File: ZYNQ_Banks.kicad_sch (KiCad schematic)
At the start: 15 parts, among them U1 XC7Z020-2CLG484I

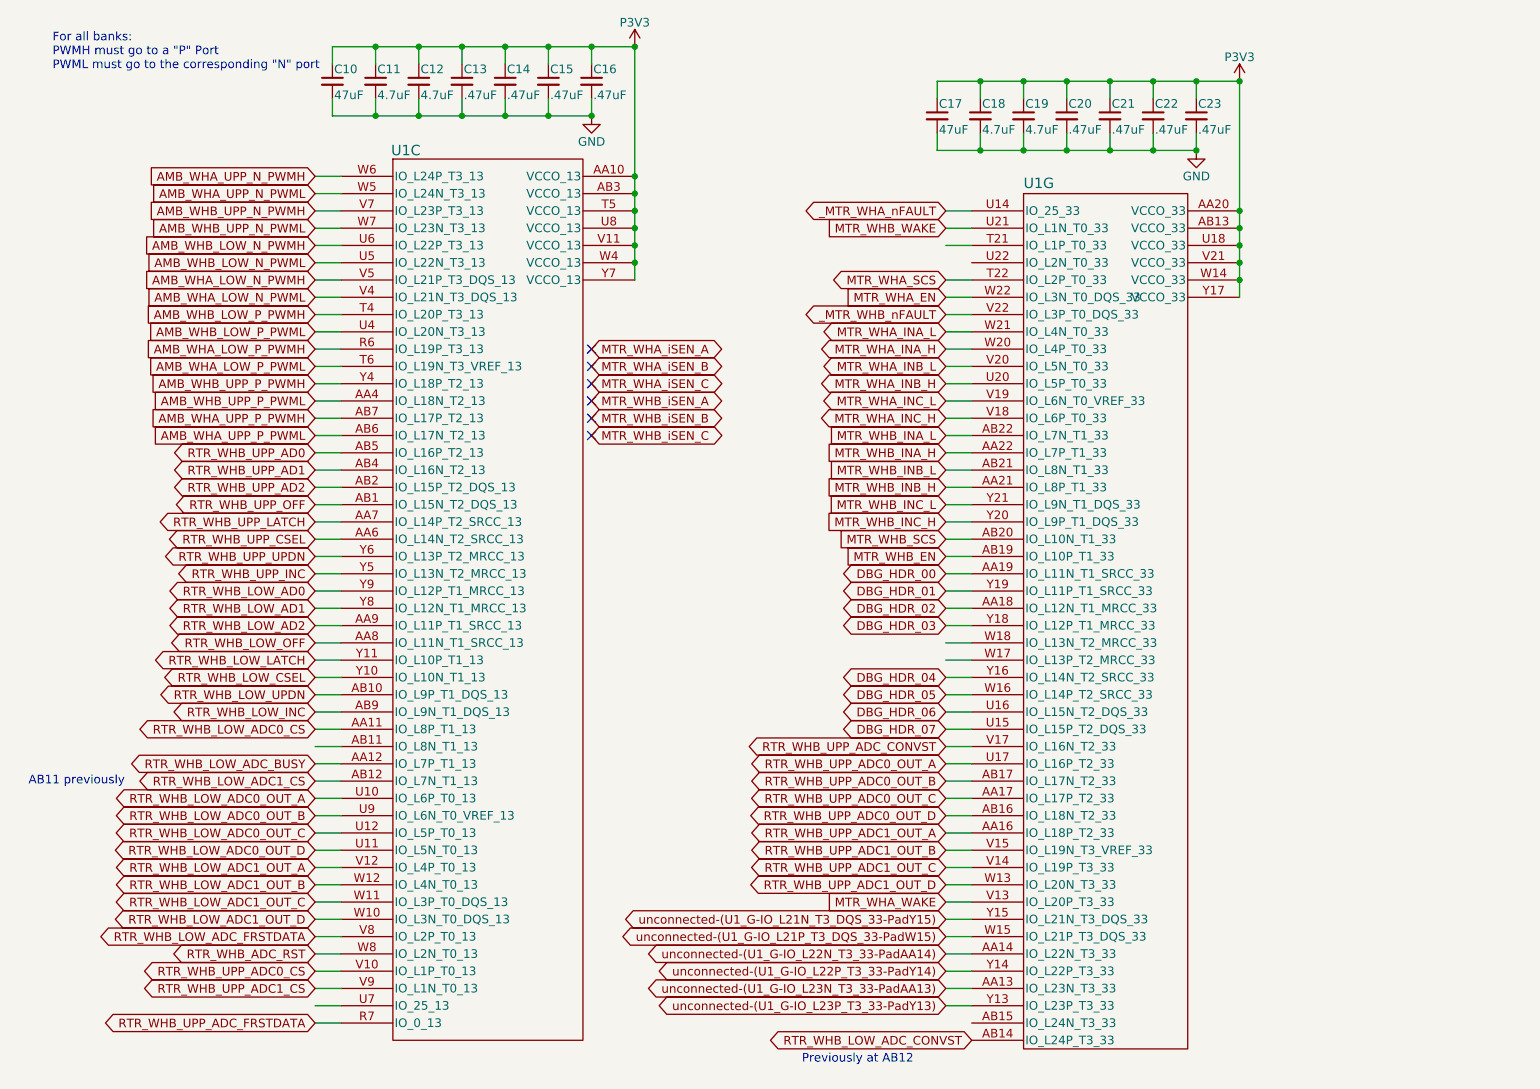
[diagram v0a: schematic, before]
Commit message: updated layouts, added motor
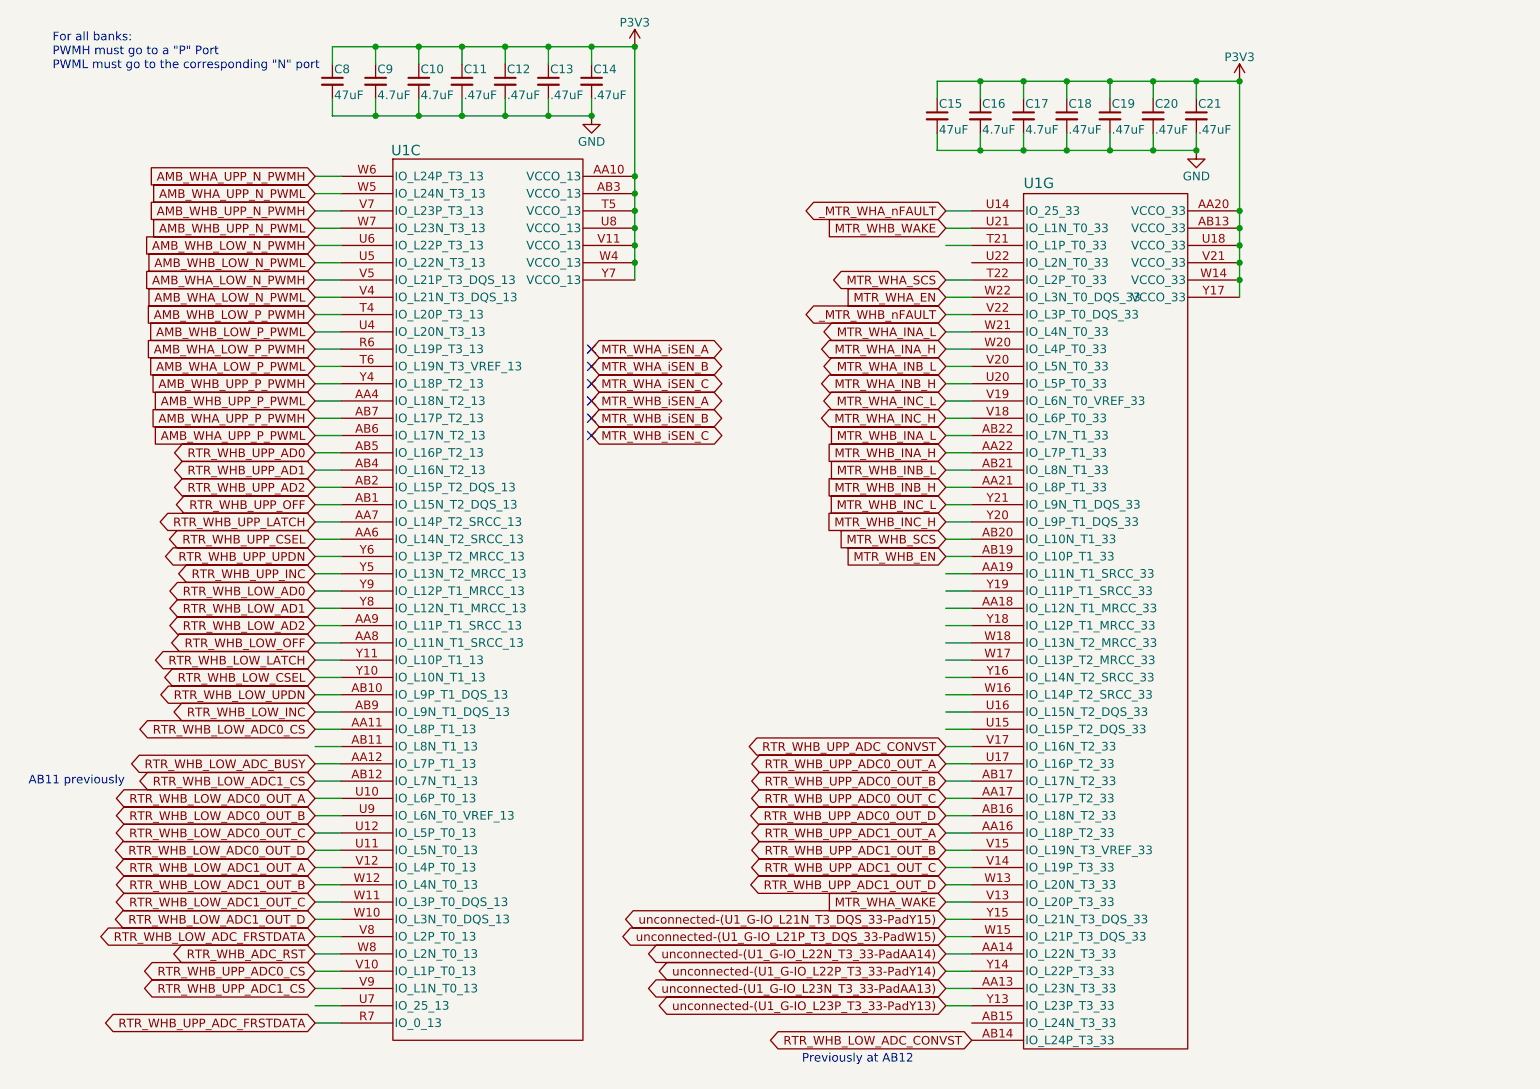
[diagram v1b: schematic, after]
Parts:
- renumbered C12 to C10, C13 to C11, C14 to C12, C15 to C13, C16 to C14, C17 to C15, C18 to C16, C19 to C17, C20 to C18, C21 to C19, C22 to C20, C23 to C21, C10 to C8, C11 to C9
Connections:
- net DBG_HDR_00: no longer names the net of U1.AA19 (IO_L11N_T1_SRCC_33)
- net DBG_HDR_01: no longer names the net of U1.Y19 (IO_L11P_T1_SRCC_33)
- net DBG_HDR_02: no longer names the net of U1.AA18 (IO_L12N_T1_MRCC_33)
- net DBG_HDR_03: no longer names the net of U1.Y18 (IO_L12P_T1_MRCC_33)
- net DBG_HDR_04: no longer names the net of U1.Y16 (IO_L14N_T2_SRCC_33)
- net DBG_HDR_05: no longer names the net of U1.W16 (IO_L14P_T2_SRCC_33)
- net DBG_HDR_06: no longer names the net of U1.U16 (IO_L15N_T2_DQS_33)
- net DBG_HDR_07: no longer names the net of U1.U15 (IO_L15P_T2_DQS_33)

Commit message: Changes to layout pins
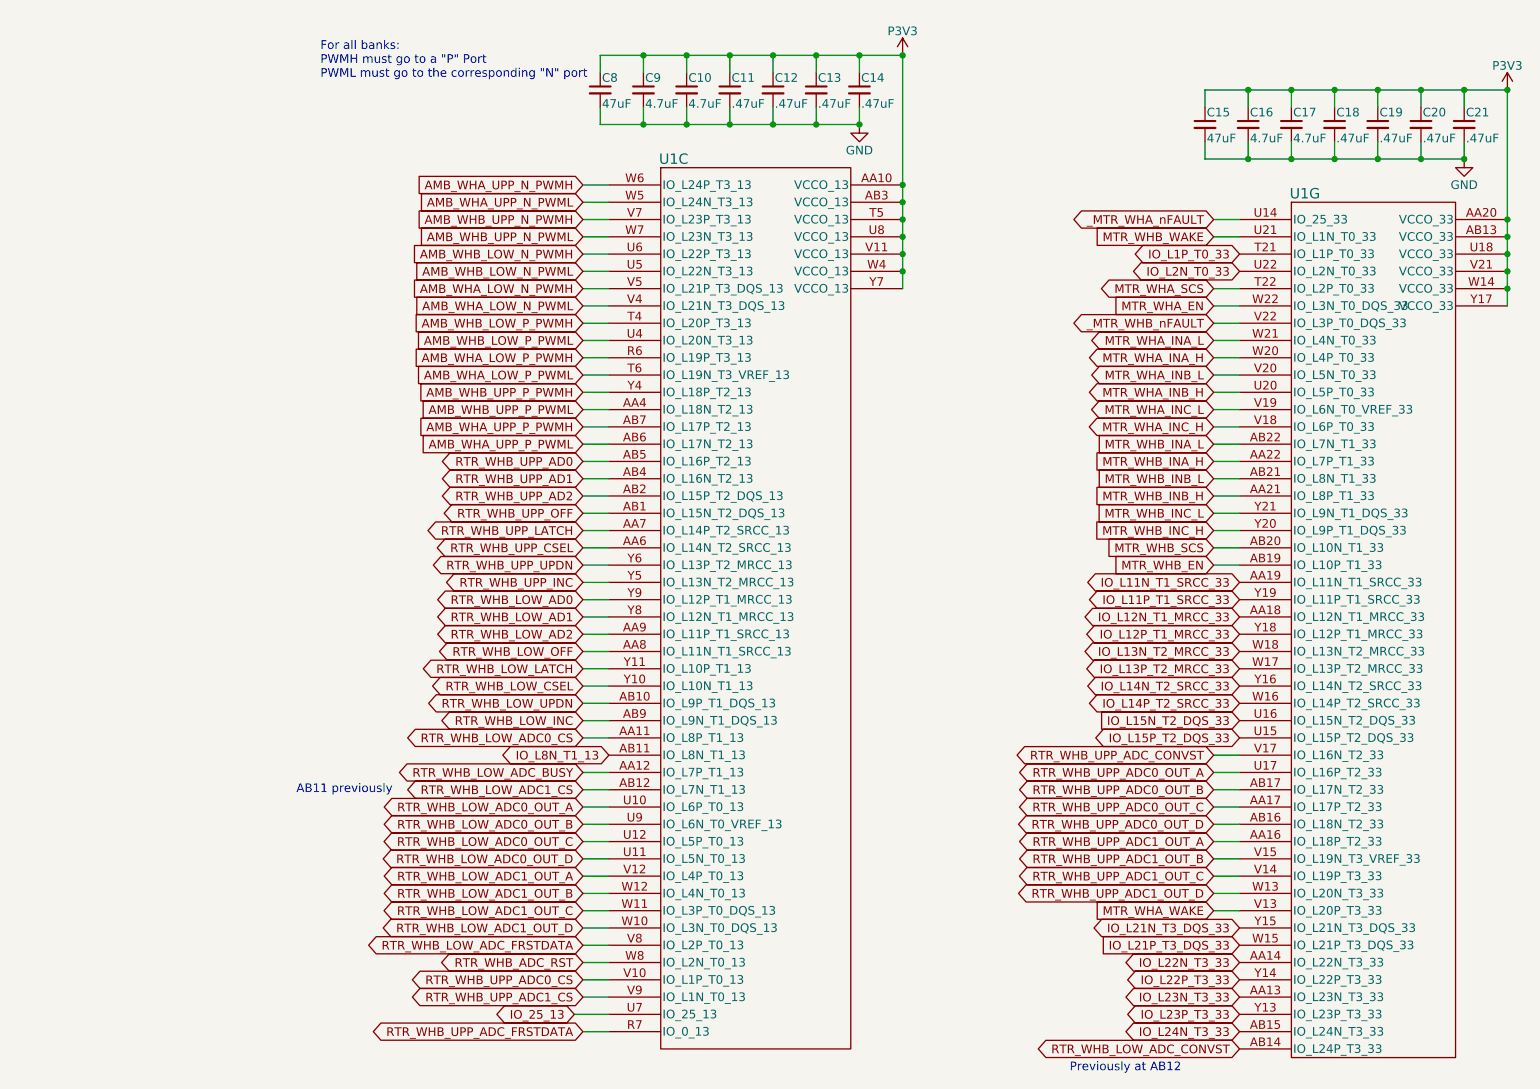
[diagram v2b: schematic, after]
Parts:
- U1: footprint DFTcustom:BGA-484_19.0x19.0mm_Layout22x22_P0.80mm_dia0.40mm -> FPGA:BGA-484_19.0x19.0mm_Layout22x22_P0.80mm_dia0.40mm
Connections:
- net IO_L8N_T1_13: now reaches U1.AB11 (IO_L8N_T1_13)
- net IO_25_13: now reaches U1.U7 (IO_25_13)
- net IO_L12N_T1_MRCC_33: now reaches U1.AA18 (IO_L12N_T1_MRCC_33)
- net IO_L11N_T1_SRCC_33: now reaches U1.AA19 (IO_L11N_T1_SRCC_33)
- net IO_L24N_T3_33: now reaches U1.AB15 (IO_L24N_T3_33)
- net IO_L1P_T0_33: now reaches U1.T21 (IO_L1P_T0_33)
- net IO_L15P_T2_DQS_33: now reaches U1.U15 (IO_L15P_T2_DQS_33)
- net IO_L15N_T2_DQS_33: now reaches U1.U16 (IO_L15N_T2_DQS_33)
- net IO_L2N_T0_33: now reaches U1.U22 (IO_L2N_T0_33)
- net IO_L14P_T2_SRCC_33: now reaches U1.W16 (IO_L14P_T2_SRCC_33)
- net IO_L13P_T2_MRCC_33: now reaches U1.W17 (IO_L13P_T2_MRCC_33)
- net IO_L13N_T2_MRCC_33: now reaches U1.W18 (IO_L13N_T2_MRCC_33)
- net IO_L14N_T2_SRCC_33: now reaches U1.Y16 (IO_L14N_T2_SRCC_33)
- net IO_L12P_T1_MRCC_33: now reaches U1.Y18 (IO_L12P_T1_MRCC_33)
- net IO_L11P_T1_SRCC_33: now reaches U1.Y19 (IO_L11P_T1_SRCC_33)
- net unconnected-(U1_G-IO_L21N_T3_DQS_33-PadY15) renamed IO_L21N_T3_DQS_33
- net unconnected-(U1_G-IO_L21P_T3_DQS_33-PadW15) renamed IO_L21P_T3_DQS_33
- net unconnected-(U1_G-IO_L22N_T3_33-PadAA14) renamed IO_L22N_T3_33
- net unconnected-(U1_G-IO_L22P_T3_33-PadY14) renamed IO_L22P_T3_33
- net unconnected-(U1_G-IO_L23N_T3_33-PadAA13) renamed IO_L23N_T3_33
- net unconnected-(U1_G-IO_L23P_T3_33-PadY13) renamed IO_L23P_T3_33
- no-connect marks 6 -> 0
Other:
- moved on the sheet: C10, C11, C12, C13, C14, C15, C16, C17, C18, C19, C20, C21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
